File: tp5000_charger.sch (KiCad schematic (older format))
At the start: 23 parts, among them J1 VIN, J2 GND, J3 VOUT, J4 GND, J5 BAT+, J6 BAT-, U1 TP5000, U2 DW01, U3 FS8205A

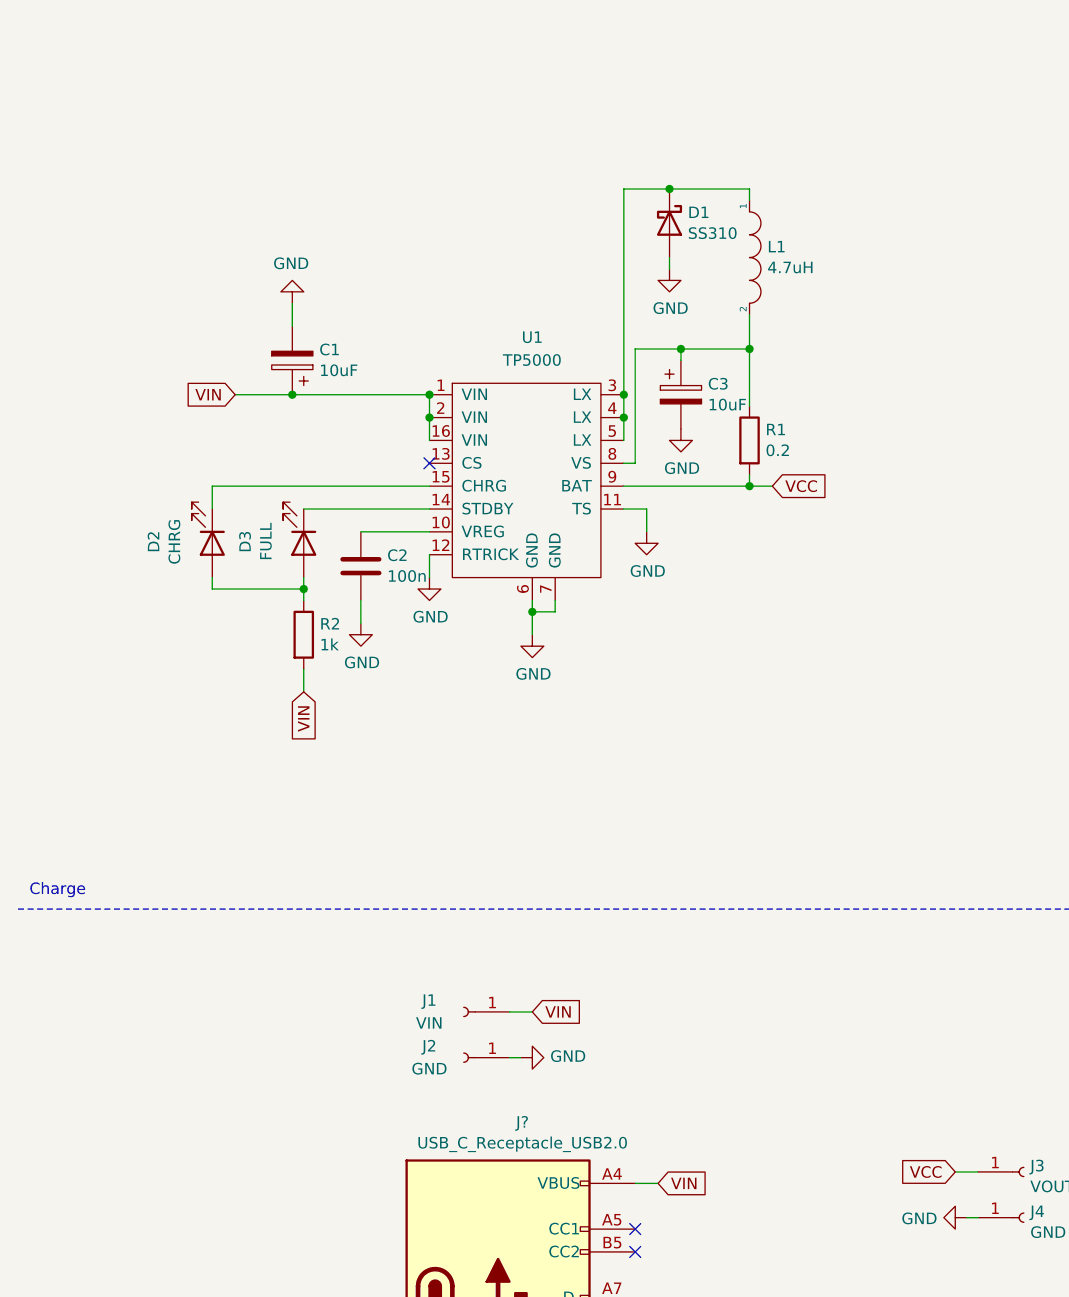
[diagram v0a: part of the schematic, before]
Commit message: select 3.6 vs 4.2V
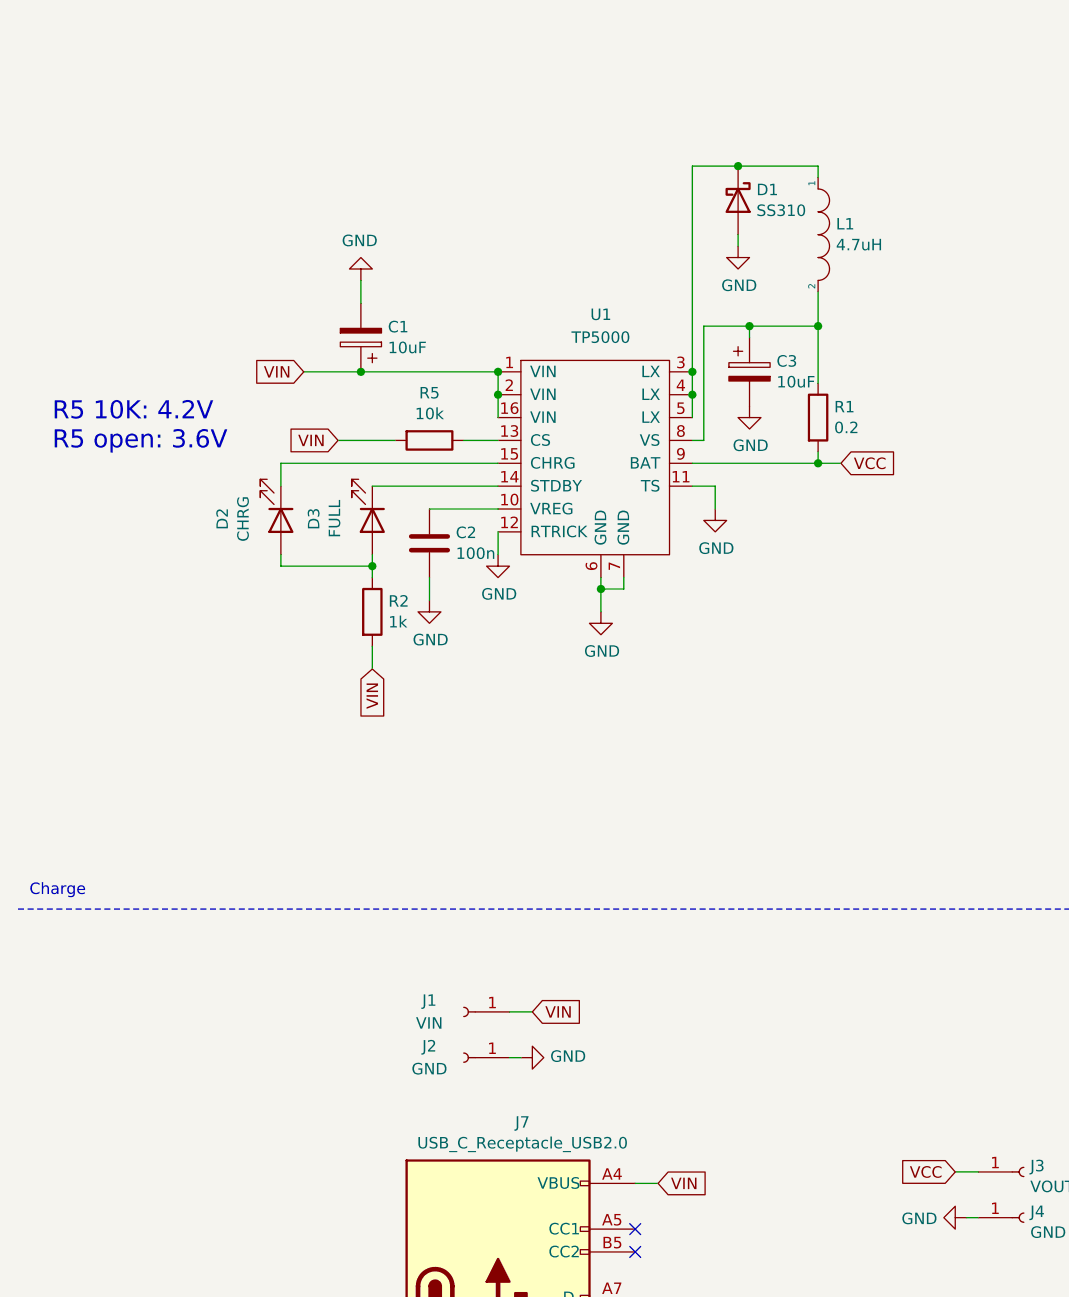
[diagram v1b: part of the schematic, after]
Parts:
- added R5: 10k, symbol Device:R
- gave numbers to parts that had none: 1
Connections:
- net VIN: now also R5.2
- net at U1.13 (CS): now also R5.1
- no-connect marks 8 -> 7
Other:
- note added: "R5 10K: 4.2V\nR5 open: 3.6V"
- moved on the sheet: C1, C2, C3, D1, D2, D3, L1, R1, R2, U1

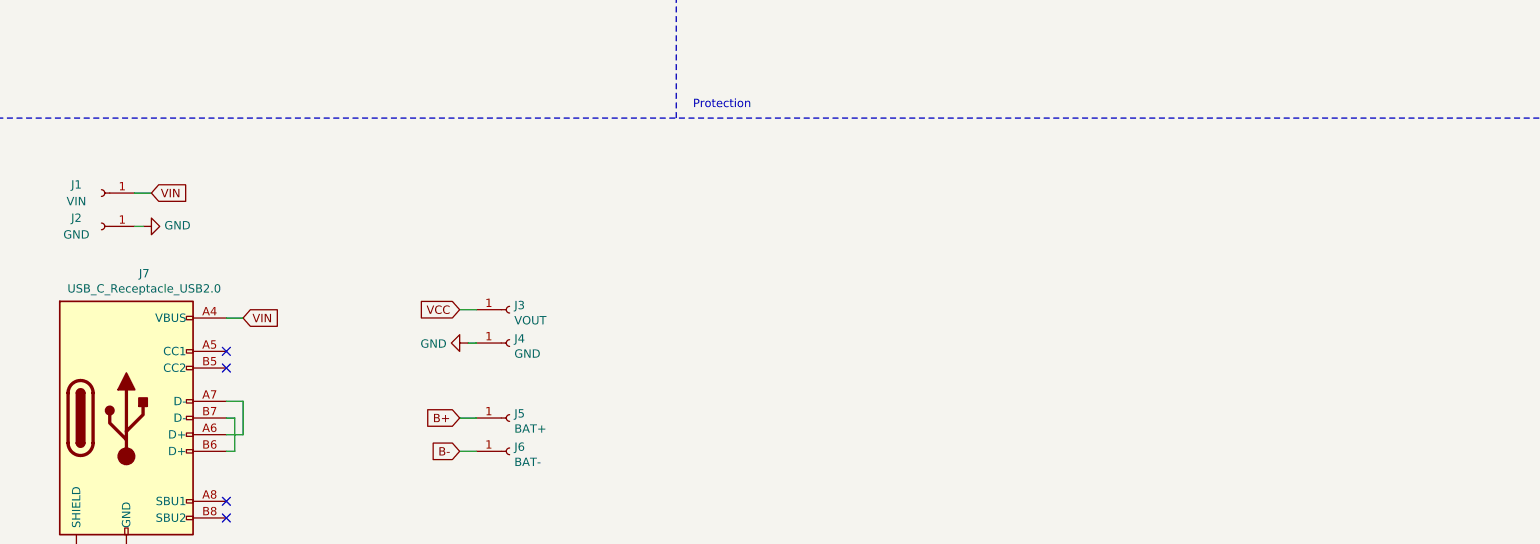
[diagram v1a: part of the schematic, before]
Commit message: mounting holes
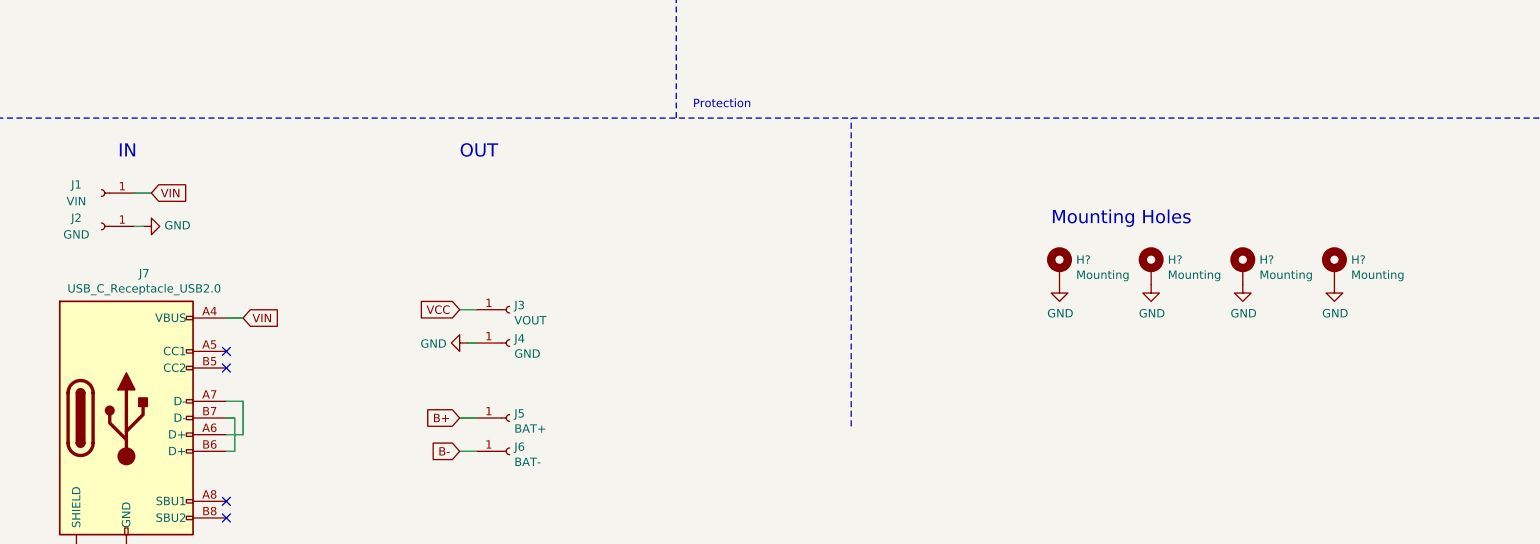
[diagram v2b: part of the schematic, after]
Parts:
- added H? (x4): Mounting, MountingHole:MountingHole_2.7mm_M2.5_DIN965_Pad, symbol Mechanical:MountingHole_Pad
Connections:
- net GND: now also H?.1, H?.1, H?.1, H?.1
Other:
- note added: "IN"
- note added: "Mounting Holes"
- note added: "OUT"
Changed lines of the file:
@@
 Text Notes 650  2700 0    79   ~ 0
 R5 10K: 4.2V\nR5 open: 3.6V
+$Comp
+L Mechanical:MountingHole_Pad H?
+U 1 1 6412FF6C
+P 8200 5600
+F 0 "H?" H 8300 5649 50  0000 L CNN
+F 1 "Mounting" H 8300 5558 50  0000 L CNN
+F 2 "MountingHole:MountingHole_2.7mm_M2.5_DIN965_Pad" H 8200 5600 50  0001 C CNN
+F 3 "~" H 8200 5600 50  0001 C CNN
+	1    8200 5600
+	1    0    0    -1
+$EndComp
+$Comp
+L Mechanical:MountingHole_Pad H?
+U 1 1 64131BF9
+P 8750 5600
+F 0 "H?" H 8850 5649 50  0000 L CNN
+F 1 "Mounting" H 8850 5558 50  0000 L CNN
+F 2 "MountingHole:MountingHole_2.7mm_M2.5_DIN965_Pad" H 8750 5600 50  0001 C CNN
+F 3 "~" H 8750 5600 50  0001 C CNN
+	1    8750 5600
+	1    0    0    -1
+$EndComp
+$Comp
+L Mechanical:MountingHole_Pad H?
+U 1 1 64134462
+P 9300 5600
+F 0 "H?" H 9400 5649 50  0000 L CNN
+F 1 "Mounting" H 9400 5558 50  0000 L CNN
+F 2 "MountingHole:MountingHole_2.7mm_M2.5_DIN965_Pad" H 9300 5600 50  0001 C CNN
+F 3 "~" H 9300 5600 50  0001 C CNN
+	1    9300 5600
+	1    0    0    -1
+$EndComp
+$Comp
+L Mechanical:MountingHole_Pad H?
+U 1 1 64136CA7
+P 9850 5600
+F 0 "H?" H 9950 5649 50  0000 L CNN
+F 1 "Mounting" H 9950 5558 50  0000 L CNN
+F 2 "MountingHole:MountingHole_2.7mm_M2.5_DIN965_Pad" H 9850 5600 50  0001 C CNN
+F 3 "~" H 9850 5600 50  0001 C CNN
+	1    9850 5600
+	1    0    0    -1
+$EndComp
+$Comp
+L power:GND #PWR?
+U 1 1 64139426
+P 8200 5700
+F 0 "#PWR?" H 8200 5450 50  0001 C CNN
+F 1 "GND" H 8205 5527 50  0000 C CNN
+F 2 "" H 8200 5700 50  0001 C CNN
+F 3 "" H 8200 5700 50  0001 C CNN
+	1    8200 5700
+	1    0    0    -1
+$EndComp
+$Comp
+L power:GND #PWR?
+U 1 1 64139DEF
+P 8750 5700
+F 0 "#PWR?" H 8750 5450 50  0001 C CNN
+F 1 "GND" H 8755 5527 50  0000 C CNN
+F 2 "" H 8750 5700 50  0001 C CNN
+F 3 "" H 8750 5700 50  0001 C CNN
+	1    8750 5700
+	1    0    0    -1
+$EndComp
+$Comp
+L power:GND #PWR?
+U 1 1 6413C473
+P 9300 5700
+F 0 "#PWR?" H 9300 5450 50  0001 C CNN
+F 1 "GND" H 9305 5527 50  0000 C CNN
+F 2 "" H 9300 5700 50  0001 C CNN
+F 3 "" H 9300 5700 50  0001 C CNN
+	1    9300 5700
+	1    0    0    -1
+$EndComp
+$Comp
+L power:GND #PWR?
+U 1 1 6413EC35
+P 9850 5700
+F 0 "#PWR?" H 9850 5450 50  0001 C CNN
+F 1 "GND" H 9855 5527 50  0000 C CNN
+F 2 "" H 9850 5700 50  0001 C CNN
+F 3 "" H 9850 5700 50  0001 C CNN
+	1    9850 5700
+	1    0    0    -1
+$EndComp
+Text Notes 8150 5350 0    79   ~ 0
+Mounting Holes
+Text Notes 2550 4950 0    79   ~ 0
+IN
+Text Notes 4600 4950 0    79   ~ 0
+OUT
+Wire Notes Line
+	6950 6550 6950 4700
 $EndSCHEMATC

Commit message: pcb design V1.1
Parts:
- C1, C3, C5: footprint Capacitor_Tantalum_SMD:CP_EIA-3216-12_Kemet-S_Pad1.58x1.35mm_HandSolder -> Capacitor_Tantalum_SMD:CP_EIA-3216-12_Kemet-S
- C2, C4: footprint Capacitor_SMD:C_0805_2012Metric_Pad1.18x1.45mm_HandSolder -> Capacitor_SMD:C_0805_2012Metric
- D2, D3: footprint LED_SMD:LED_0805_2012Metric_Pad1.15x1.40mm_HandSolder -> LED_SMD:LED_0805_2012Metric
- J7: footprint (none) -> Connector_USB:USB_C_Receptacle_Palconn_UTC16-G
- L1: footprint Inductor_SMD:L_Taiyo-Yuden_NR-50xx_HandSoldering -> Inductor_SMD:L_Taiyo-Yuden_NR-50xx
- R2, R3, R4: footprint Resistor_SMD:R_0805_2012Metric_Pad1.20x1.40mm_HandSolder -> Resistor_SMD:R_0805_2012Metric
- R5: footprint (none) -> Resistor_SMD:R_0805_2012Metric
- gave numbers to parts that had none: 4
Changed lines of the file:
@@
 F 0 "R4" V 9243 1850 50  0000 C CNN
 F 1 "100" V 9334 1850 50  0000 C CNN
-F 2 "Resistor_SMD:R_0805_2012Metric_Pad1.20x1.40mm_HandSolder" V 9380 1850 50  0001 C CNN
+F 2 "Resistor_SMD:R_0805_2012Metric" V 9380 1850 50  0001 C CNN
 F 3 "" H 9450 1850 50  0001 C CNN
 	1    9450 1850
@@
 F 0 "C4" H 9165 2046 50  0000 L CNN
 F 1 "100nF" H 9165 1955 50  0000 L CNN
-F 2 "Capacitor_SMD:C_0805_2012Metric_Pad1.18x1.45mm_HandSolder" H 9088 1850 50  0001 C CNN
+F 2 "Capacitor_SMD:C_0805_2012Metric" H 9088 1850 50  0001 C CNN
 F 3 "~" H 9050 2000 50  0001 C CNN
 	1    9050 2000
@@
 F 0 "R3" V 7243 2050 50  0000 C CNN
 F 1 "1k" V 7334 2050 50  0000 C CNN
-F 2 "Resistor_SMD:R_0805_2012Metric_Pad1.20x1.40mm_HandSolder" V 7380 2050 50  0001 C CNN
+F 2 "Resistor_SMD:R_0805_2012Metric" V 7380 2050 50  0001 C CNN
 F 3 "~" H 7450 2050 50  0001 C CNN
 	1    7450 2050
@@
 F 0 "C1" H 1882 2154 50  0000 R CNN
 F 1 "10uF" H 1882 2245 50  0000 R CNN
-F 2 "Capacitor_Tantalum_SMD:CP_EIA-3216-12_Kemet-S_Pad1.58x1.35mm_HandSolder" H 2038 2050 50  0001 C CNN
+F 2 "Capacitor_Tantalum_SMD:CP_EIA-3216-12_Kemet-S" H 2038 2050 50  0001 C CNN
 F 3 "https://www.lcsc.com/product-detail/Tantalum-Capacitors_CEC-Shenzhen-Zhenhua-XinYun-Elec-CA45A-A-16V-10uF-K_C129279.html" H 2000 2200 50  0001 C CNN
 	1    2000 2200
@@
 F 0 "C2" H 2415 3146 50  0000 L CNN
 F 1 "100n" H 2415 3055 50  0000 L CNN
-F 2 "Capacitor_SMD:C_0805_2012Metric_Pad1.18x1.45mm_HandSolder" H 2338 2950 50  0001 C CNN
+F 2 "Capacitor_SMD:C_0805_2012Metric" H 2338 2950 50  0001 C CNN
 F 3 "~" H 2300 3100 50  0001 C CNN
 	1    2300 3100
@@
 F 0 "C3" H 3818 2396 50  0000 L CNN
 F 1 "10uF" H 3818 2305 50  0000 L CNN
-F 2 "Capacitor_Tantalum_SMD:CP_EIA-3216-12_Kemet-S_Pad1.58x1.35mm_HandSolder" H 3738 2200 50  0001 C CNN
+F 2 "Capacitor_Tantalum_SMD:CP_EIA-3216-12_Kemet-S" H 3738 2200 50  0001 C CNN
 F 3 "https://www.lcsc.com/product-detail/Tantalum-Capacitors_CEC-Shenzhen-Zhenhua-XinYun-Elec-CA45A-A-16V-10uF-K_C129279.html" H 3700 2350 50  0001 C CNN
 	1    3700 2350
@@
 F 0 "L1" V 3954 1828 50  0000 L CNN
 F 1 "4.7uH" V 4045 1828 50  0000 L CNN
-F 2 "Inductor_SMD:L_Taiyo-Yuden_NR-50xx_HandSoldering" H 4000 1750 50  0001 C CNN
+F 2 "Inductor_SMD:L_Taiyo-Yuden_NR-50xx" H 4000 1750 50  0001 C CNN
 F 3 "https://www.lcsc.com/product-detail/Inductors-SMD_SHOU-HAN-CY54-4-7UH_C2929429.html" H 4000 1750 50  0001 C CNN
 	1    4000 1750
@@
 F 0 "C5" H 9818 2196 50  0000 L CNN
 F 1 "10uF" H 9818 2105 50  0000 L CNN
-F 2 "Capacitor_Tantalum_SMD:CP_EIA-3216-12_Kemet-S_Pad1.58x1.35mm_HandSolder" H 9738 2000 50  0001 C CNN
+F 2 "Capacitor_Tantalum_SMD:CP_EIA-3216-12_Kemet-S" H 9738 2000 50  0001 C CNN
 F 3 "https://www.lcsc.com/product-detail/Tantalum-Capacitors_CEC-Shenzhen-Zhenhua-XinYun-Elec-CA45A-A-16V-10uF-K_C129279.html" H 9700 2150 50  0001 C CNN
 	1    9700 2150
@@
 F 0 "R2" H 2120 3446 50  0000 L CNN
 F 1 "1k" H 2120 3355 50  0000 L CNN
-F 2 "Resistor_SMD:R_0805_2012Metric_Pad1.20x1.40mm_HandSolder" V 1980 3400 50  0001 C CNN
+F 2 "Resistor_SMD:R_0805_2012Metric" V 1980 3400 50  0001 C CNN
 F 3 "~" H 2050 3400 50  0001 C CNN
 	1    2050 3400
@@
 F 0 "D3" H 2043 2745 50  0000 C CNN
 F 1 "FULL" H 2043 2836 50  0000 C CNN
-F 2 "LED_SMD:LED_0805_2012Metric_Pad1.15x1.40mm_HandSolder" H 2050 3000 50  0001 C CNN
+F 2 "LED_SMD:LED_0805_2012Metric" H 2050 3000 50  0001 C CNN
 F 3 "~" H 2050 3000 50  0001 C CNN
 	1    2050 3000
@@
 F 0 "D2" H 1643 2745 50  0000 C CNN
 F 1 "CHRG" H 1643 2836 50  0000 C CNN
-F 2 "LED_SMD:LED_0805_2012Metric_Pad1.15x1.40mm_HandSolder" H 1650 3000 50  0001 C CNN
+F 2 "LED_SMD:LED_0805_2012Metric" H 1650 3000 50  0001 C CNN
 F 3 "~" H 1650 3000 50  0001 C CNN
 	1    1650 3000
@@
 F 0 "J7" H 2707 7367 50  0000 C CNN
 F 1 "USB_C_Receptacle_USB2.0" H 2707 7276 50  0000 C CNN
-F 2 "" H 2750 6500 50  0001 C CNN
+F 2 "Connector_USB:USB_C_Receptacle_Palconn_UTC16-G" H 2750 6500 50  0001 C CNN
 F 3 "https://www.usb.org/sites/default/files/documents/usb_type-c.zip" H 2750 6500 50  0001 C CNN
 	1    2600 6500
@@
 F 0 "R5" V 2093 2650 50  0000 C CNN
 F 1 "10k" V 2184 2650 50  0000 C CNN
-F 2 "" V 2230 2650 50  0001 C CNN
+F 2 "Resistor_SMD:R_0805_2012Metric" V 2230 2650 50  0001 C CNN
 F 3 "~" H 2300 2650 50  0001 C CNN
 	1    2300 2650
@@
 R5 10K: 4.2V\nR5 open: 3.6V
 $Comp
-L Mechanical:MountingHole_Pad H?
+L Mechanical:MountingHole_Pad H1
 U 1 1 6412FF6C
 P 8200 5600
-F 0 "H?" H 8300 5649 50  0000 L CNN
+F 0 "H1" H 8300 5649 50  0000 L CNN
 F 1 "Mounting" H 8300 5558 50  0000 L CNN
 F 2 "MountingHole:MountingHole_2.7mm_M2.5_DIN965_Pad" H 8200 5600 50  0001 C CNN
@@
 $EndComp
 $Comp
-L Mechanical:MountingHole_Pad H?
+L Mechanical:MountingHole_Pad H2
 U 1 1 64131BF9
 P 8750 5600
-F 0 "H?" H 8850 5649 50  0000 L CNN
+F 0 "H2" H 8850 5649 50  0000 L CNN
 F 1 "Mounting" H 8850 5558 50  0000 L CNN
 F 2 "MountingHole:MountingHole_2.7mm_M2.5_DIN965_Pad" H 8750 5600 50  0001 C CNN
@@
 $EndComp
 $Comp
-L Mechanical:MountingHole_Pad H?
+L Mechanical:MountingHole_Pad H3
 U 1 1 64134462
 P 9300 5600
-F 0 "H?" H 9400 5649 50  0000 L CNN
+F 0 "H3" H 9400 5649 50  0000 L CNN
 F 1 "Mounting" H 9400 5558 50  0000 L CNN
 F 2 "MountingHole:MountingHole_2.7mm_M2.5_DIN965_Pad" H 9300 5600 50  0001 C CNN
@@
 $EndComp
 $Comp
-L Mechanical:MountingHole_Pad H?
+L Mechanical:MountingHole_Pad H4
 U 1 1 64136CA7
 P 9850 5600
-F 0 "H?" H 9950 5649 50  0000 L CNN
+F 0 "H4" H 9950 5649 50  0000 L CNN
 F 1 "Mounting" H 9950 5558 50  0000 L CNN
 F 2 "MountingHole:MountingHole_2.7mm_M2.5_DIN965_Pad" H 9850 5600 50  0001 C CNN
@@
 $EndComp
 $Comp
-L power:GND #PWR?
+L power:GND #PWR02
 U 1 1 64139426
 P 8200 5700
-F 0 "#PWR?" H 8200 5450 50  0001 C CNN
+F 0 "#PWR02" H 8200 5450 50  0001 C CNN
 F 1 "GND" H 8205 5527 50  0000 C CNN
 F 2 "" H 8200 5700 50  0001 C CNN
@@
 $EndComp
 $Comp
-L power:GND #PWR?
+L power:GND #PWR016
 U 1 1 64139DEF
 P 8750 5700
-F 0 "#PWR?" H 8750 5450 50  0001 C CNN
+F 0 "#PWR016" H 8750 5450 50  0001 C CNN
 F 1 "GND" H 8755 5527 50  0000 C CNN
 F 2 "" H 8750 5700 50  0001 C CNN
@@
 $EndComp
 $Comp
-L power:GND #PWR?
+L power:GND #PWR017
 U 1 1 6413C473
 P 9300 5700
-F 0 "#PWR?" H 9300 5450 50  0001 C CNN
+F 0 "#PWR017" H 9300 5450 50  0001 C CNN
 F 1 "GND" H 9305 5527 50  0000 C CNN
 F 2 "" H 9300 5700 50  0001 C CNN
@@
 $EndComp
 $Comp
-L power:GND #PWR?
+L power:GND #PWR018
 U 1 1 6413EC35
 P 9850 5700
-F 0 "#PWR?" H 9850 5450 50  0001 C CNN
+F 0 "#PWR018" H 9850 5450 50  0001 C CNN
 F 1 "GND" H 9855 5527 50  0000 C CNN
 F 2 "" H 9850 5700 50  0001 C CNN

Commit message: layout smaller
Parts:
- removed H3, H4: Mounting, MountingHole:MountingHole_2.7mm_M2.5_DIN965_Pad, symbol Mechanical:MountingHole_Pad
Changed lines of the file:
@@
-$EndComp
-$Comp
-L Mechanical:MountingHole_Pad H3
-U 1 1 64134462
-P 9300 5600
-F 0 "H3" H 9400 5649 50  0000 L CNN
-F 1 "Mounting" H 9400 5558 50  0000 L CNN
-F 2 "MountingHole:MountingHole_2.7mm_M2.5_DIN965_Pad" H 9300 5600 50  0001 C CNN
-F 3 "~" H 9300 5600 50  0001 C CNN
-	1    9300 5600
-	1    0    0    -1
-$EndComp
-$Comp
-L Mechanical:MountingHole_Pad H4
-U 1 1 64136CA7
-P 9850 5600
-F 0 "H4" H 9950 5649 50  0000 L CNN
-F 1 "Mounting" H 9950 5558 50  0000 L CNN
-F 2 "MountingHole:MountingHole_2.7mm_M2.5_DIN965_Pad" H 9850 5600 50  0001 C CNN
-F 3 "~" H 9850 5600 50  0001 C CNN
-	1    9850 5600
-	1    0    0    -1
 $EndComp
 $Comp
@@
 	1    0    0    -1
 $EndComp
-$Comp
-L power:GND #PWR017
-U 1 1 6413C473
-P 9300 5700
-F 0 "#PWR017" H 9300 5450 50  0001 C CNN
-F 1 "GND" H 9305 5527 50  0000 C CNN
-F 2 "" H 9300 5700 50  0001 C CNN
-F 3 "" H 9300 5700 50  0001 C CNN
-	1    9300 5700
-	1    0    0    -1
-$EndComp
-$Comp
-L power:GND #PWR018
-U 1 1 6413EC35
-P 9850 5700
-F 0 "#PWR018" H 9850 5450 50  0001 C CNN
-F 1 "GND" H 9855 5527 50  0000 C CNN
-F 2 "" H 9850 5700 50  0001 C CNN
-F 3 "" H 9850 5700 50  0001 C CNN
-	1    9850 5700
-	1    0    0    -1
-$EndComp

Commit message: version number 1.2
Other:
- note added: "1.2"
- note removed: "1"
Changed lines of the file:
@@
 $EndBitmap
 Text Notes 10600 7650 0    79   ~ 0
-1
+1.2
 Text Notes 8200 7650 0    79   ~ 0
 31.01.2023
